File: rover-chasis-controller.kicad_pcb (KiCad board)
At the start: 2 copper layers, 86 x 97 mm, 79 parts, among them J1 Motor control, J11 Compass Connection (I2C), J15 External LED (Red), J16 External LED (Yellow), J17 External LED (Green), J2 Motor control, J22 Ultrasonic Sensor Inputs, J3 Motor control, J38 Motor control, J4 Screw_Terminal_01x02, J40 Encoder, J41 Encoder, J42 Encoder, J43 Encoder, J7 TTL, J8 Ultrasonic Sensor Inputs, Q14 MMBT3904_C181119, Q2 HSBA100P04_C2987717, Q33 MMBT3904_C181119, Q34 MMBT3904_C181119, Q35 MMBT3904_C181119, U1 APT2012LVBC/D, U2 APT2012LVBC/D, U3 APT2012LVBC/D, U4 AP64500, U5 MPU-6050_C24112, U6 PCA9685PW,118, U7 APT2012LVBC/D

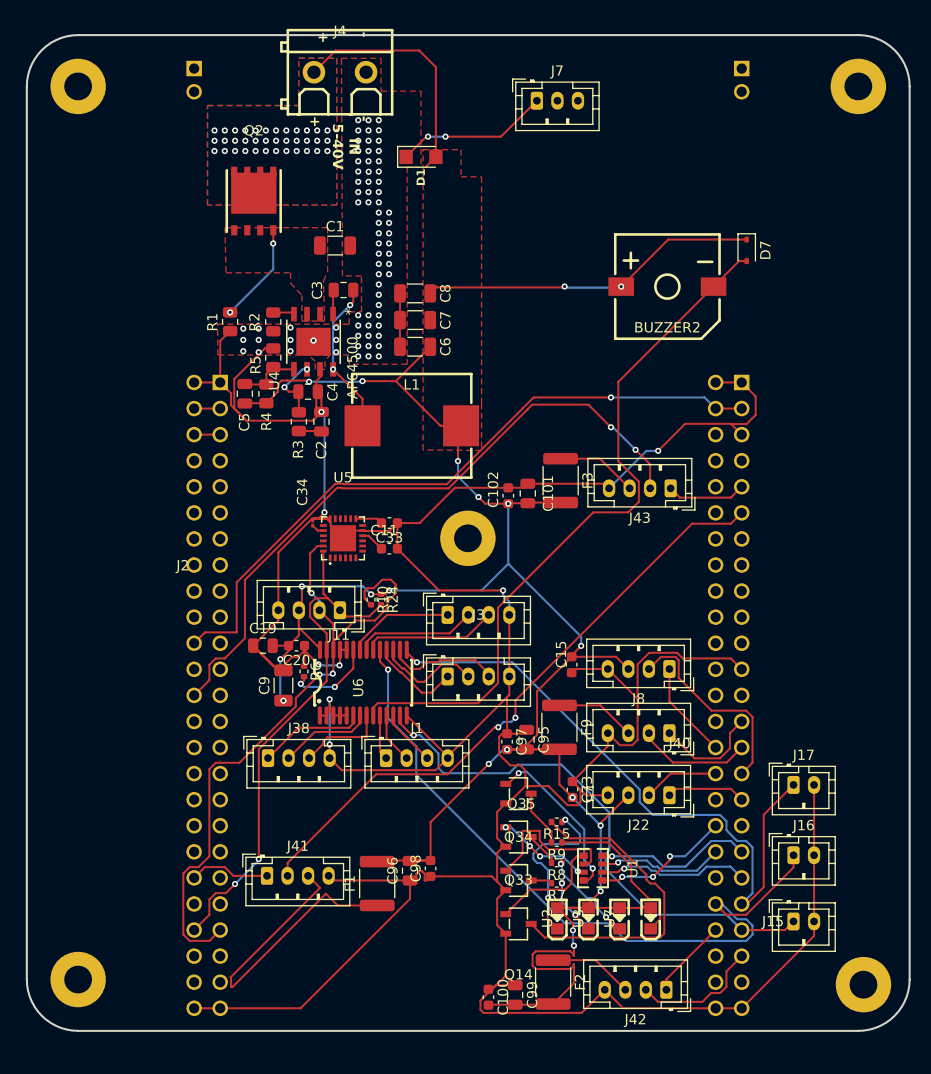
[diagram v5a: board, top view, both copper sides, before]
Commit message: Issue #1: Corrected some mistakes
Solved short circuit problems, replaced components smaller that 0805, adjusted references on the pcb design, connected TTL connector to STM32, added missing schematic to measure input voltage
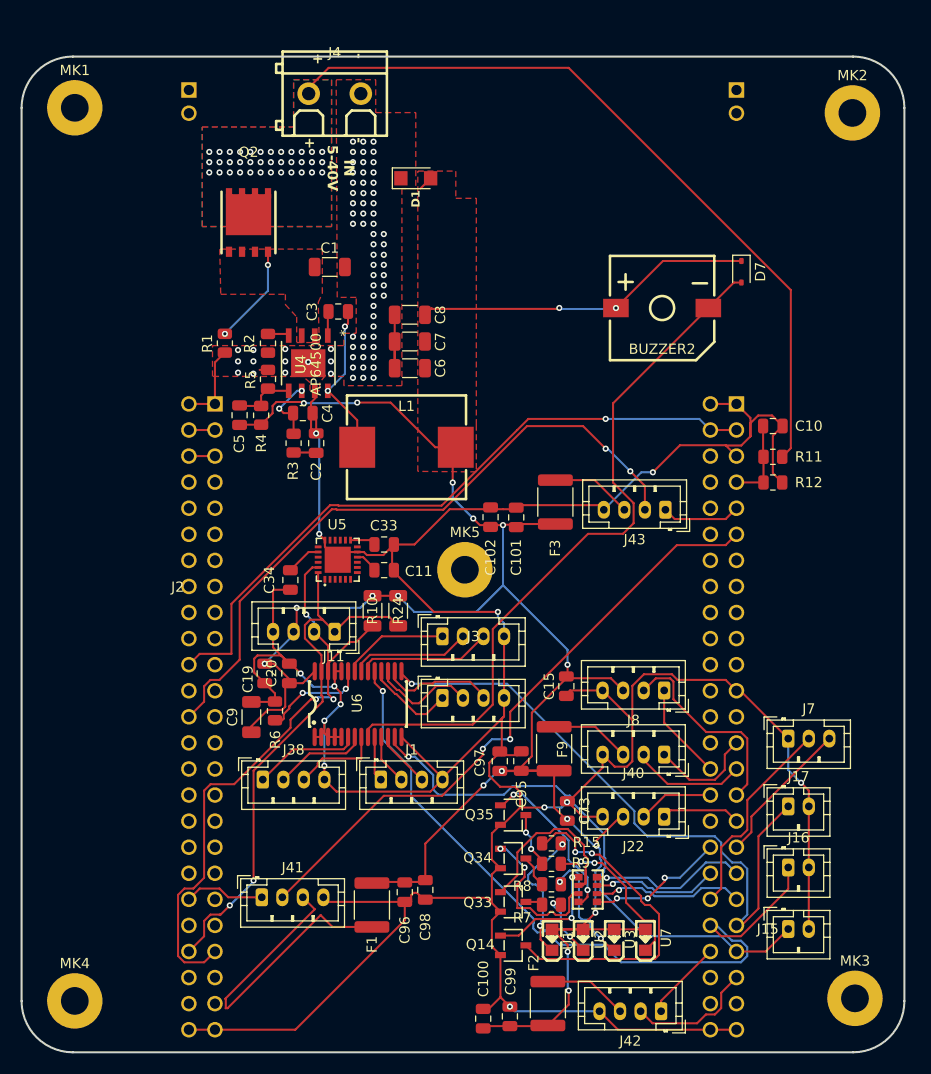
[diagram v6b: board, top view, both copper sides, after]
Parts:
- removed the MK1 at (113.3, 133.5)
- removed the MK1 at (112.8, 46.0)
- removed the MK1 at (74.8, 90.0)
- removed the MK1 at (36.8, 46.0)
- removed the MK1 at (36.8, 133.0)
- added C10: 0.1uF, Capacitor_SMD:C_0805_2012Metric, F.Cu at (104.5, 79.1)
- added MK1: M2.5, MountingHole:MountingHole_2.7mm_M2.5_Pad, F.Cu at (36.5, 48.1)
- added MK2: M2.5, MountingHole:MountingHole_2.7mm_M2.5_Pad, F.Cu at (112.2, 48.6)
- added MK3: M2.5, MountingHole:MountingHole_2.7mm_M2.5_Pad, F.Cu at (112.5, 134.8)
- added MK4: M2.5, MountingHole:MountingHole_2.7mm_M2.5_Pad, F.Cu at (36.5, 135.1)
- added MK5: M2.5, MountingHole:MountingHole_2.7mm_M2.5_Pad, F.Cu at (74.5, 93.1)
- added R11: 100k, Resistor_SMD:R_0805_2012Metric, F.Cu at (104.5, 82.1)
- added R12: 22k, Resistor_SMD:R_0805_2012Metric, F.Cu at (104.5, 84.6)
- C100, C102, C11, C15, C20, C33, C73, C97, C98: footprint Capacitor_SMD:C_0603_1608Metric -> Capacitor_SMD:C_0805_2012Metric
- C101, C95, C96, C99: value 10 uF -> 10uF
- C3: value 100nF -> 0.1uF
- C34: footprint Capacitor_SMD:C_01005_0402Metric -> Capacitor_SMD:C_0805_2012Metric
- C6, C7, C8: value 22 uF -> 22uF
- R10, R24: footprint Resistor_SMD:R_0402_1005Metric -> Resistor_SMD:R_1206_3216Metric
- R15, R6, R7, R8, R9: footprint Resistor_SMD:R_0402_1005Metric -> Resistor_SMD:R_0805_2012Metric
- moved J7 66.8 mm to (106.0, 109.5)
- moved C34 5.96 mm to (57.5, 94.1), turned to -90 degrees
- moved R6 4.77 mm to (56.0, 106.8)
- moved C9 4.38 mm to (53.7, 107.4)
- moved C20 2.79 mm to (57.4, 103.2), turned to -90 degrees
- moved C102 2.71 mm to (77.0, 88.0)
- moved C19 2.71 mm to (55.0, 103.2), turned to 90 degrees
- moved C101 2.59 mm to (79.5, 88.0)
- moved BUZZER2 2.15 mm to (93.7, 67.6)
- moved C99 2.15 mm to (78.9, 136.6)
- moved C5 2.15 mm to (52.5, 78.0)
- moved R2 2.15 mm to (55.3, 71.0)
- moved R5 2.15 mm to (55.3, 74.5)
- moved C100 2.15 mm to (76.3, 136.8)
- moved D7 2.15 mm to (101.4, 64.1)
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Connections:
- J4 pad 1: VCC (5V) -> VCC (12V)
- Q2 pad 5: VCC (5V) -> VCC (12V)
- TB1 pad P1_35: unconnected-(TB1-PB11-PadP1_35) -> /TTL_RX
- TB1 pad P1_40: unconnected-(TB1-PD8-PadP1_40) -> /TTL_TX
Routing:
- net VCC (12V): track 0.00 -> 73.7 mm, vias 0 -> 36
- net GND: track 415.1 -> 374.3 mm, vias 82 -> 85
- net VCC (5V): track 268.5 -> 235.0 mm, vias 56 -> 19
- net /TTL_TX: track 0.00 -> 20.1 mm
- net /TTL_RX: track 0.00 -> 14.3 mm
- net /POWER_SUPPLY_ADC: track 0.00 -> 8.16 mm
- net /SCL: track 67.9 -> 60.3 mm
- net /transistor_array4/B3: track 9.41 -> 15.9 mm, vias 4 -> 2
- net /transistor_array4/B2: track 14.5 -> 19.4 mm
- net Net-(U3-K): track 9.24 -> 11.9 mm
- net /SDA: track 51.5 -> 54.0 mm
- net Net-(U5-CPOUT): track 1.24 -> 3.44 mm
- net Net-(U1-K): track 16.3 -> 14.1 mm
- net /LED_Collector_1: track 31.8 -> 33.6 mm, vias 0 -> 2
- net Net-(U6-~{OE}): track 8.63 -> 10.4 mm
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- added copper zone on B.Cu, net VCC (12V)
- added copper zone on F.Cu, net VCC (12V)
- removed copper zone on B.Cu, net VCC (5V)

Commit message: Issue #1: Prepare for production
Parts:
- added G***: LOGO, kpi-rover:kpi-rover-logo, F.Cu at (37.8, 123.2)
- C16: renamed from C95; value 10uF -> 10uFx16V
- C17: renamed from C101; value 10uF -> 10uFx16V
- C21: renamed from C9; value 10uF -> 10uFx16V; footprint Capacitor_SMD:C_1206_3216Metric -> Capacitor_SMD:C_0805_2012Metric
- C22: renamed from C96; value 10uF -> 10uFx16V
- C23: renamed from C99; value 10uF -> 10uFx16V
- C3: renamed from C1; value 10uF -> 10uFx50V
- C5: renamed from C19; value 10uF -> 10uFx16V
- R5: renamed from R24; footprint Resistor_SMD:R_1206_3216Metric -> Resistor_SMD:R_0805_2012Metric
- R6: renamed from R10; footprint Resistor_SMD:R_1206_3216Metric -> Resistor_SMD:R_0805_2012Metric
- moved R14 13.0 mm to (66.9, 99.8), turned to 180 degrees
- moved C1 3.46 mm to (104.5, 82.5)
- moved C4 2.47 mm to (55.1, 102.4), turned to 0 degrees
- moved R5 2.33 mm to (65.7, 96.9)
- moved R6 2.21 mm to (67.7, 96.9)
- moved C21 1.70 mm to (55.1, 106.4), turned to 180 degrees
- moved R1 1.57 mm to (104.4, 80.5)
- moved C5 1.21 mm to (55.0, 104.4), turned to 0 degrees
- moved C24 0.18 mm to (70.6, 124.5)
- moved C25 0.16 mm to (76.3, 136.7)
- renumbered BUZZER2 to BUZZER1, C10 to C1, C4 to C10, C5 to C11, C15 to C12, C6 to C13, C7 to C14, C8 to C15, C73 to C18, C97 to C19, C11 to C2, C102 to C20, C98 to C24, C100 to C25, C20 to C4, C33 to C6, C34 to C7, C2 to C8, C3 to C9, D7 to D1, D1 to D2, F9 to F1, F3 to F2, F1 to F3, F2 to F4, J17 to J1, J40 to J10, J43 to J11, J22 to J12, J1 to J13, J3 to J14, J41 to J15, J42 to J16, J16 to J2, J15 to J3, J11 to J5, J7 to J6, J8 to J7, J38 to J8, J2 to J9, MK5 to MK1, MK1 to MK2, MK2 to MK3, MK3 to MK4, MK4 to MK5, Q2 to Q1, Q14 to Q2, Q33 to Q3, Q34 to Q4, Q35 to Q5, R11 to R1, R15 to R10, R7 to R11, R8 to R12, R9 to R13, R6 to R14, R12 to R2, R1 to R3, R2 to R4, R3 to R7, R4 to R8, R5 to R9, U5 to U1, U4 to U2, U1 to U3, U2 to U4, U3 to U5, U7 to U6, U6 to U7
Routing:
- net GND: track 374.3 -> 170.1 mm, vias 85 -> 80
- net Net-(TB1-VDD-PadP1_3): track 66.6 -> 0.00 mm, vias 1 -> 0
- net Net-(J15-Pin_3): track 33.4 -> 7.93 mm
- net /SCL: track 60.3 -> 53.1 mm, vias 3 -> 2
- net VCC (5V): track 235.0 -> 228.9 mm, vias 19 -> 15
- net Net-(U7-~{OE}): track 10.4 -> 4.68 mm, vias 2 -> 0
- net /SDA: track 54.0 -> 49.8 mm, vias 2 -> 0
- net /BUZZER_OUT: track 69.1 -> 65.9 mm, vias 0 -> 2
- net /ENC3_B: track 65.1 -> 61.9 mm
- net /transistor_array4/B2: track 19.4 -> 17.4 mm
- net Net-(U2-COMP): track 6.48 -> 4.56 mm, vias 2 -> 0
- net /POWER_SUPPLY_ADC: track 8.16 -> 6.81 mm
- net Net-(Q1-G): track 9.74 -> 10.6 mm
- net /MOTOR3_PWM: track 10.4 -> 11.2 mm
- net VCC (12V): track 73.7 -> 73.1 mm
- added copper zone on B.Cu, net GND
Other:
- board text added: "KPI Rover Chassis controller (ECU) Version: 1.0"
